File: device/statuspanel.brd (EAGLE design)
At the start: 57.1 x 66 mm, 8 parts

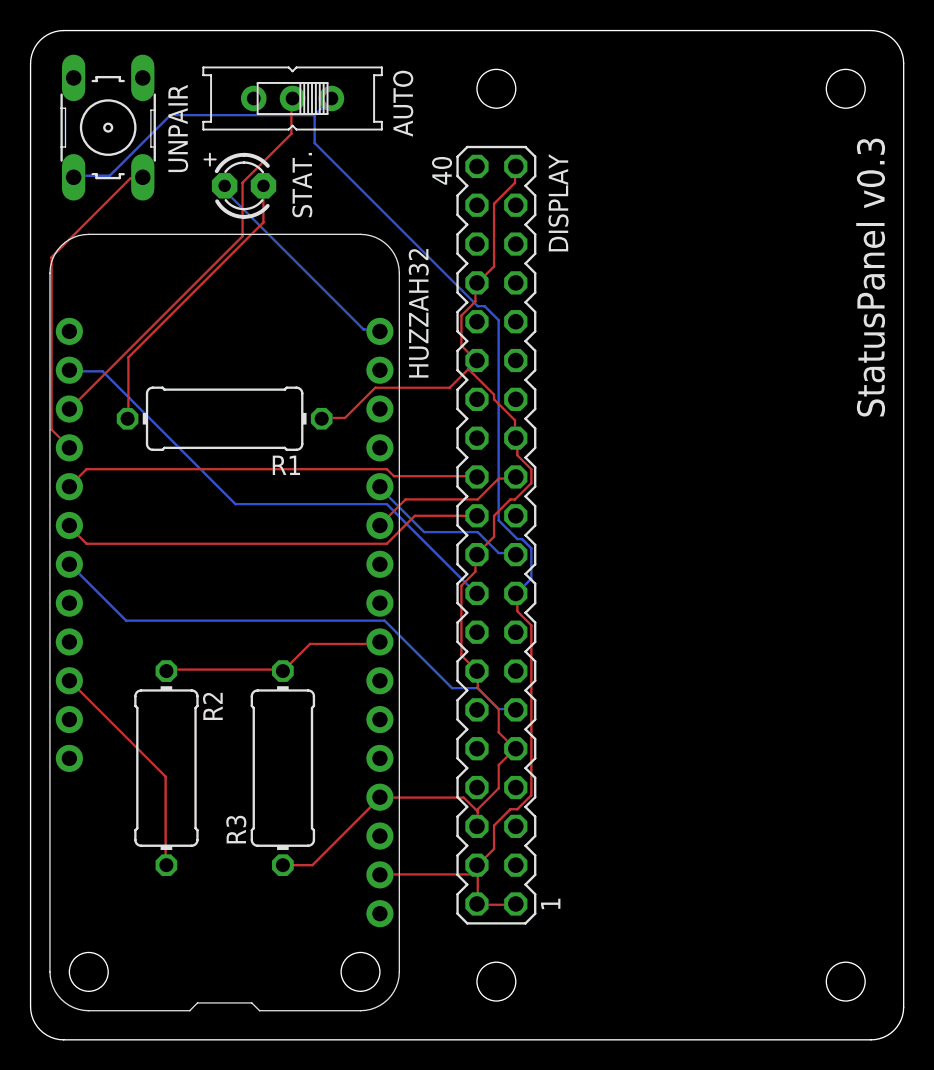
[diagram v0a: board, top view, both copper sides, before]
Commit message: feat(device): Add a reset button to the custom PCB (#379)
This also includes drive-by changes to use SMD resistors, and correct the resistance of the status LED resistor.
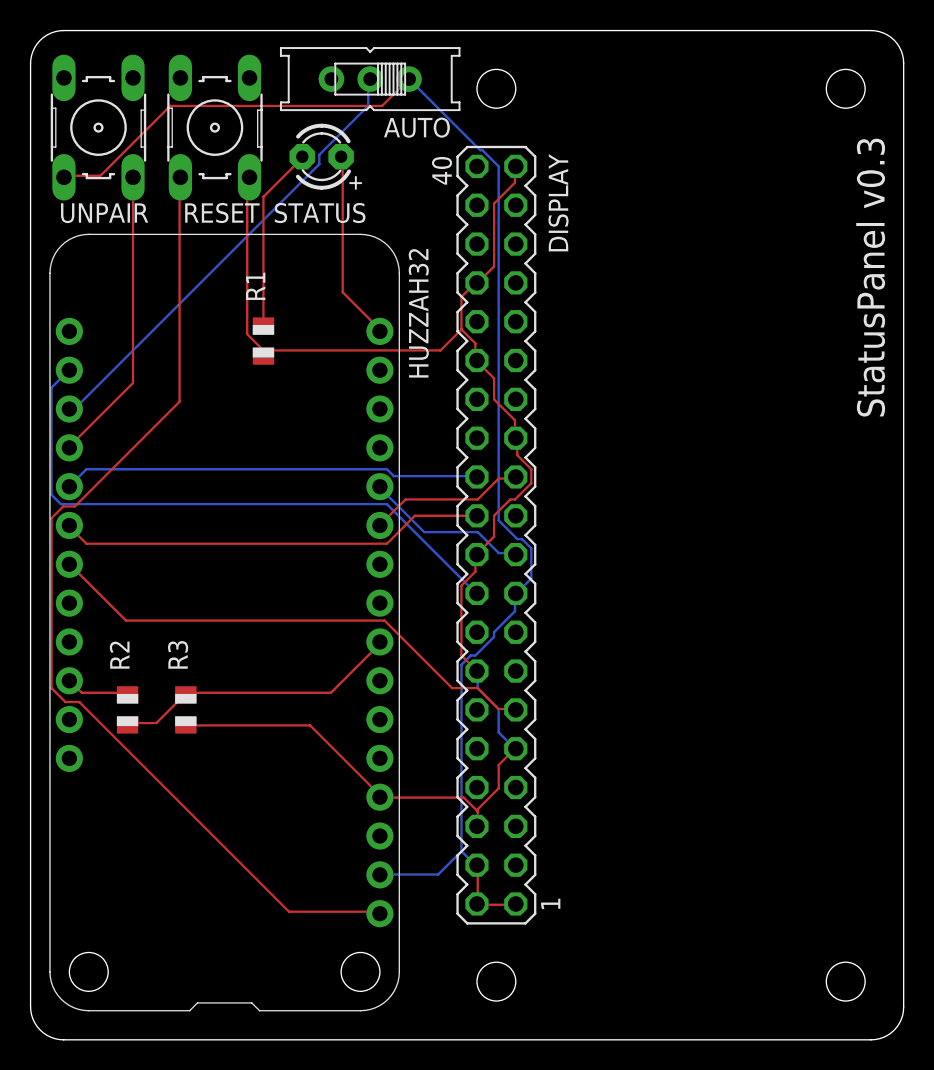
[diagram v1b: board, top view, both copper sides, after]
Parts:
- removed STAT.: (no value), adafruit:LED3MM
- added RESET: (no value), switch-omron:B3F-10XX
- added STATUS: (no value), adafruit:LED3MM
- R1: value 5.1 -> 330; device adafruit:0411/12 -> adafruit:R0805
- R2, R3: device adafruit:0411/12 -> adafruit:R0805
- moved R3 7.41 mm to (10.2, 21.6)
- moved R1 5.68 mm to (15.2, 45.7), turned to 90 degrees
- moved AUTO 5.24 mm to (22.2, 62.9)
- moved R2 4.58 mm to (6.35, 21.6), turned to 90 degrees
- moved UNPAIR 0.63 mm to (4.45, 59.7)
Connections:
- new net RST: HUZZAH32.1, RESET.1
- net GND: now also RESET.3
- net N$3: now also STATUS.K; no longer STAT..K
- net STATUS: now also STATUS.A; no longer STAT..A
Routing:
- net RST: track 0.00 -> 65.0 mm
- net GND: track 77.7 -> 98.7 mm
- net USB: track 14.7 -> 4.19 mm
- net N$3: track 18.9 -> 12.2 mm
- net BUSY: track 32.7 -> 39.1 mm
- net 3V3: track 89.2 -> 94.0 mm
- net USBDETECT: track 14.9 -> 18.9 mm
- net AUTO: track 26.4 -> 30.0 mm
- net STATUS: track 14.4 -> 12.5 mm
- net UNPAIR: track 21.1 -> 19.4 mm
